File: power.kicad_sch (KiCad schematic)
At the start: 108 parts, among them U1 LT8350RV#PBF, U2 MP2386GG, U3 TPS65983BAZBHR

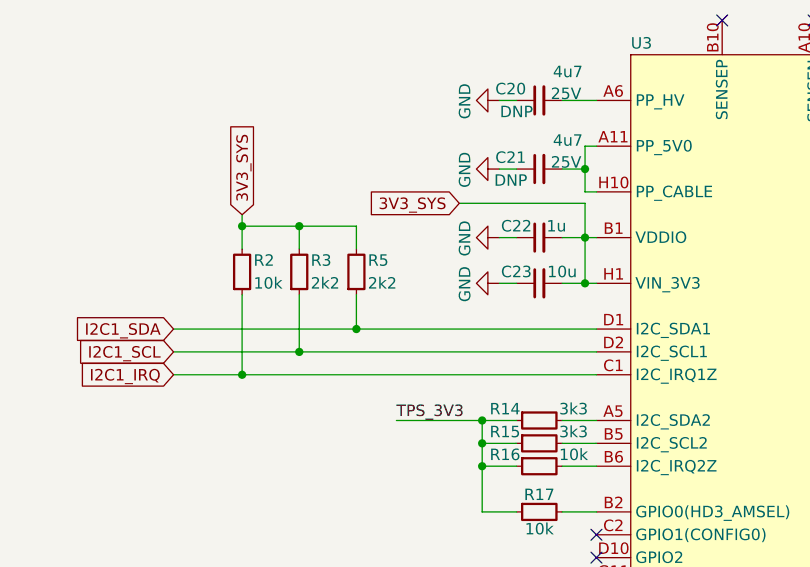
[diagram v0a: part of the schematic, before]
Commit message: Finished placement and routing of all TB controller related passives, finished routing of TB signals
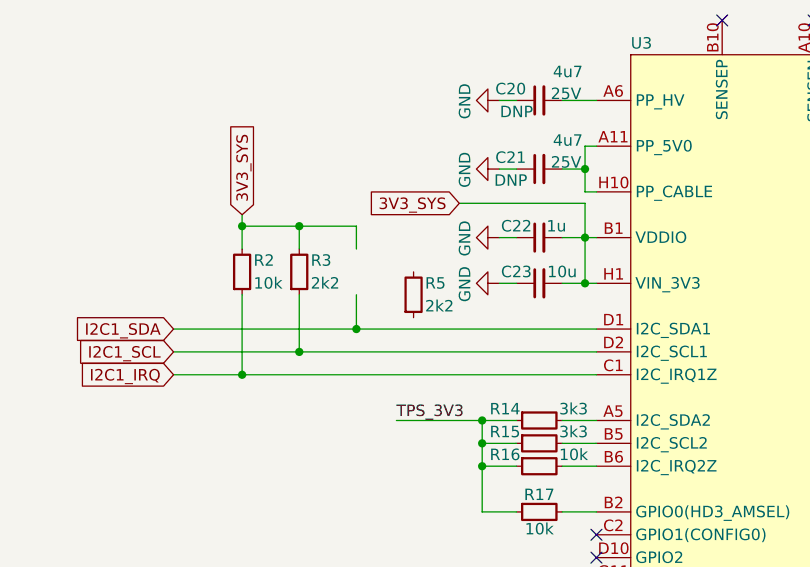
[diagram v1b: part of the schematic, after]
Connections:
- net 3V3_SYS: no longer R5.2
- net I2C1_SDA: no longer R5.1
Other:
- moved on the sheet: R5
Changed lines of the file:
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@@
     (pin "1")
   )
-  (symbol (lib_name "R_2k2_0402_1") (lib_id "antmicroResistors0402:R_2k2_0402") (at 95.25 68.58 90) (unit 1)
+  (symbol (lib_name "R_2k2_0402_1") (lib_id "antmicroResistors0402:R_2k2_0402") (at 101.6 71.12 90) (unit 1)
     (in_bom yes) (on_board yes)
-    (property "Reference" "R5" (id 0) (at 96.52 64.77 90)
+    (property "Reference" "R5" (id 0) (at 102.87 67.31 90)
       (effects (font (size 1.27 1.27) (thickness 0.15)) (justify right))
     )
-    (property "Value" "R_2k2_0402" (id 1) (at 107.95 48.26 0)
+    (property "Value" "R_2k2_0402" (id 1) (at 114.3 50.8 0)
       (effects (font (size 1.27 1.27) (thickness 0.15)) (justify left bottom) hide)
     )
-    (property "Footprint" "antmicro-footprints:R_0402_1005Metric" (id 2) (at 110.49 48.26 0)
+    (property "Footprint" "antmicro-footprints:R_0402_1005Metric" (id 2) (at 116.84 50.8 0)
       (effects (font (size 1.27 1.27) (thickness 0.15)) (justify left bottom) hide)
     )
-    (property "Datasheet" "https://www.bourns.com/docs/product-datasheets/cr.pdf" (id 3) (at 113.03 48.26 0)
+    (property "Datasheet" "https://www.bourns.com/docs/product-datasheets/cr.pdf" (id 3) (at 119.38 50.8 0)
       (effects (font (size 1.27 1.27) (thickness 0.15)) (justify left bottom) hide)
     )
-    (property "MPN" "CR0402-FX-2201GLF" (id 4) (at 115.57 48.26 0)
+    (property "MPN" "CR0402-FX-2201GLF" (id 4) (at 121.92 50.8 0)
       (effects (font (size 1.27 1.27) (thickness 0.15)) (justify left bottom) hide)
     )
-    (property "Manufacturer" "Bourns" (id 5) (at 118.11 48.26 0)
+    (property "Manufacturer" "Bourns" (id 5) (at 124.46 50.8 0)
       (effects (font (size 1.27 1.27) (thickness 0.15)) (justify left bottom) hide)
     )
-    (property "License" "Apache-2.0 License" (id 6) (at 120.65 48.26 0)
+    (property "License" "Apache-2.0 License" (id 6) (at 127 50.8 0)
       (effects (font (size 1.27 1.27) (thickness 0.15)) (justify left bottom) hide)
     )
-    (property "Copyright" "Copyright (c) 2023 Antmicro" (id 7) (at 123.19 48.26 0)
+    (property "Copyright" "Copyright (c) 2023 Antmicro" (id 7) (at 129.54 50.8 0)
       (effects (font (size 1.27 1.27) (thickness 0.15)) (justify left bottom) hide)
     )
-    (property "Val" "2k2" (id 8) (at 96.52 67.31 90)
+    (property "Val" "2k2" (id 8) (at 102.87 69.85 90)
       (effects (font (size 1.27 1.27) (thickness 0.15)) (justify right))
     )
-    (property "Tolerance" "1%" (id 9) (at 105.41 48.26 0)
+    (property "Tolerance" "1%" (id 9) (at 111.76 50.8 0)
       (effects (font (size 1.27 1.27)) (justify left bottom) hide)
     )

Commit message: Updated libraries, finished PCIe clock generator section
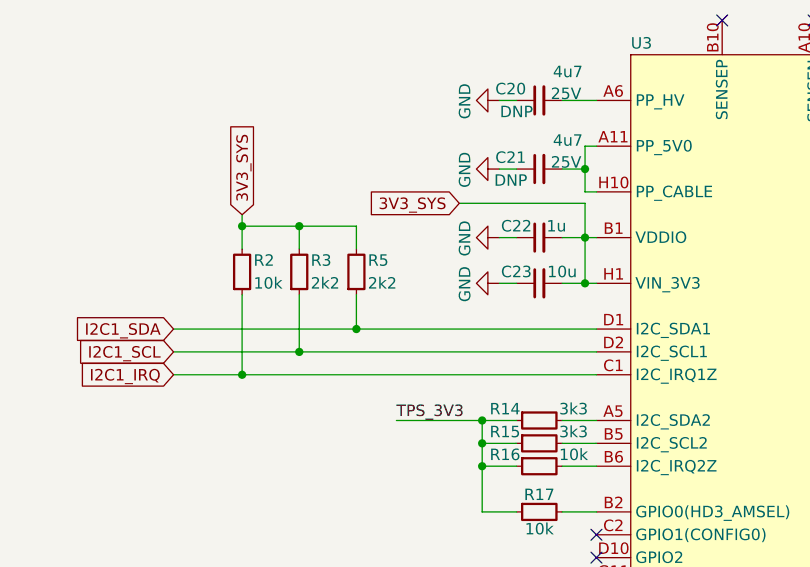
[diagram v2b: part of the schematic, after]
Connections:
- net 3V3_SYS: now also R5.2
- net I2C1_SDA: now also R5.1
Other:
- moved on the sheet: R5

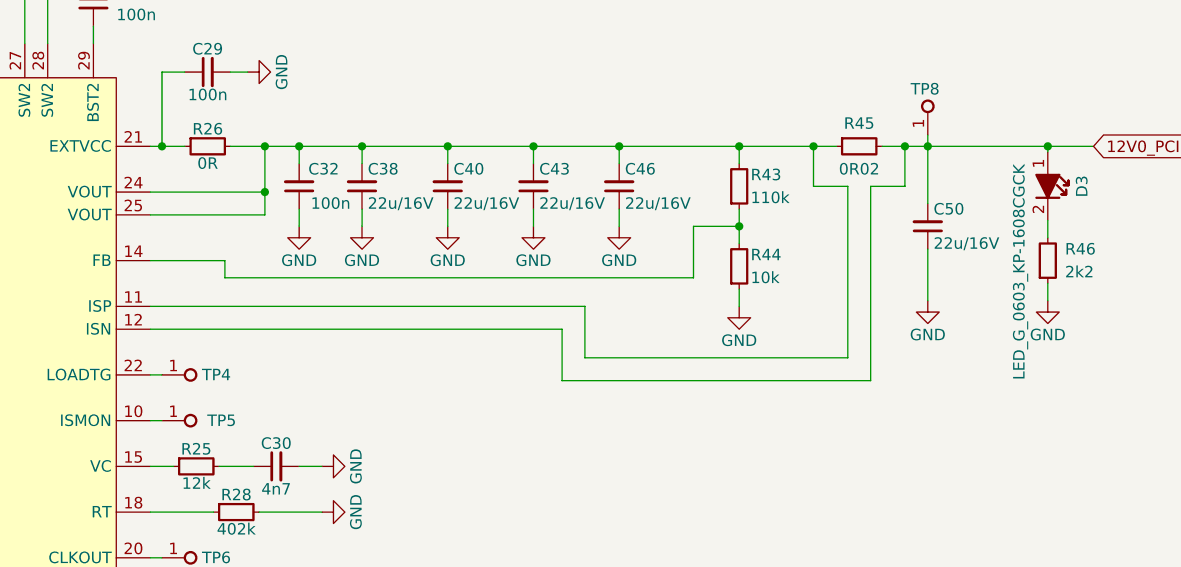
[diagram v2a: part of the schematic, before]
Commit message: Finished placing all DC-DC converters with all related components
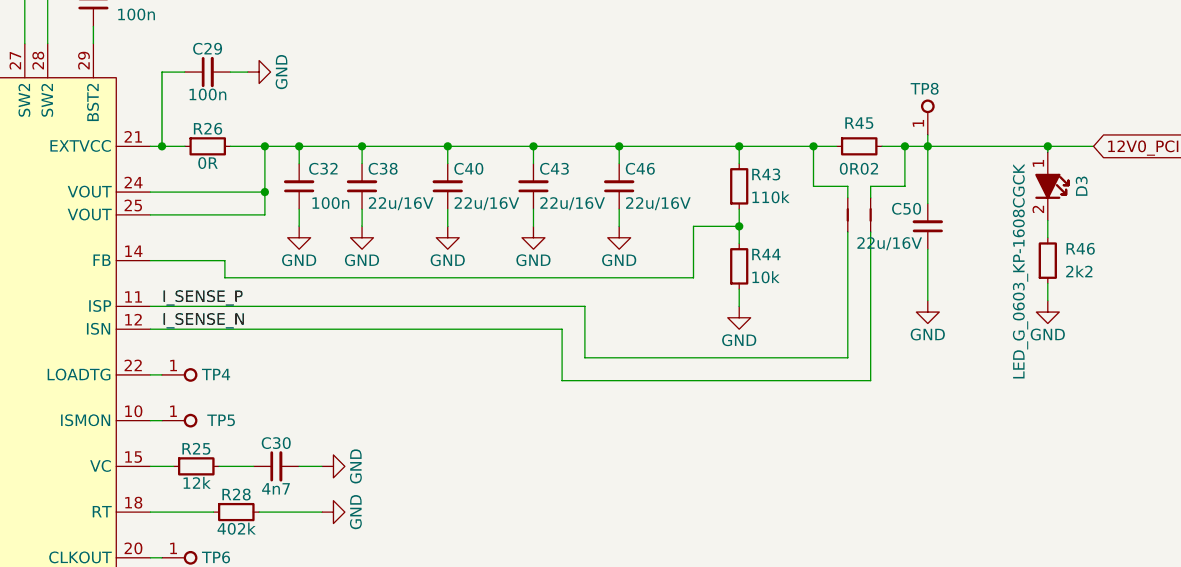
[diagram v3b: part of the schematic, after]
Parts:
- added TP10, TP11: Net-Tie_2, antmicro-footprints:NetTie-2_SMD_Pad0.127mm, symbol antmicroShuntsJumpers:Net-Tie_2
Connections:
- net 12V0_PCIE: now also TP11.2; no longer U1.12 (ISN)
- net at C32.2, C38.2, C40.2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: now also TP10.2; no longer U1.11 (ISP)
- new net I_SENSE_N: TP11.1, U1.12 (ISN)
- new net I_SENSE_P: TP10.1, U1.11 (ISP)
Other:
- moved on the sheet: C50
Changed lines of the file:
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@@
     (stroke (width 0) (type default) (color 0 0 0 0))
   )
+  (wire (pts (xy 242.57 240.03) (xy 242.57 241.3))
+    (stroke (width 0) (type default) (color 0 0 0 0))
+  )
   (wire (pts (xy 210.82 255.905) (xy 210.82 261.62))
     (stroke (width 0) (type default) (color 0 0 0 0))
@@
     (stroke (width 0) (type default) (color 0 0 0 0))
   )
+  (wire (pts (xy 245.11 245.11) (xy 245.11 261.62))
+    (stroke (width 0) (type default) (color 0 0 0 0))
+  )
   (wire (pts (xy 193.04 57.15) (xy 194.945 57.15))
     (stroke (width 0) (type default) (color 0 0 0 0))
   )
+  (wire (pts (xy 242.57 245.11) (xy 242.57 259.08))
+    (stroke (width 0) (type default) (color 0 0 0 0))
+  )
   (wire (pts (xy 120.015 148.59) (xy 121.92 148.59))
     (stroke (width 0) (type default) (color 0 0 0 0))
@@
     (stroke (width 0) (type default) (color 0 0 0 0))
   )
+  (wire (pts (xy 245.11 240.03) (xy 245.11 241.3))
+    (stroke (width 0) (type default) (color 0 0 0 0))
+  )
   (wire (pts (xy 88.9 60.96) (xy 88.9 63.5))
     (stroke (width 0) (type default) (color 0 0 0 0))
@@
     (stroke (width 0) (type default) (color 0 0 0 0))
   )
-  (wire (pts (xy 245.11 240.03) (xy 245.11 261.62))
-    (stroke (width 0) (type default) (color 0 0 0 0))
-  )
   (wire (pts (xy 149.86 344.17) (xy 152.4 344.17))
     (stroke (width 0) (type default) (color 0 0 0 0))
@@
     (stroke (width 0) (type default) (color 0 0 0 0))
   )
-  (wire (pts (xy 242.57 240.03) (xy 242.57 259.08))
-    (stroke (width 0) (type default) (color 0 0 0 0))
-  )
   (wire (pts (xy 33.655 229.87) (xy 40.005 229.87))
     (stroke (width 0) (type default) (color 0 0 0 0))
@@
     (effects (font (size 1.27 1.27)) (justify right bottom))
   )
+  (label "I_SENSE_P" (at 166.37 253.365 0)
+    (effects (font (size 1.27 1.27)) (justify left bottom))
+  )
   (label "TPS_3V3" (at 200.025 128.27 180)
     (effects (font (size 1.27 1.27)) (justify right bottom))
   )
+  (label "I_SENSE_N" (at 166.37 255.905 0)
+    (effects (font (size 1.27 1.27)) (justify left bottom))
+  )
   (label "SMPS_VREF" (at 185.42 286.385 180)
     (effects (font (size 1.27 1.27)) (justify right bottom))
@@
     (pin "2")
   )
+  (symbol (lib_id "antmicroShuntsJumpers:Net-Tie_2") (at 245.11 245.11 90) (unit 1)
+    (in_bom yes) (on_board yes) (fields_autoplaced)
+    (property "Reference" "TP11" (id 0) (at 246.38 241.9349 90)
+      (effects (font (size 1.27 1.27) (thickness 0.15)) (justify right) hide)
+    )
+    (property "Value" "Net-Tie_2" (id 1) (at 246.38 244.4749 90)
+      (effects (font (size 1.27 1.27) (thickness 0.15)) (justify right) hide)
+    )
+    (property "Footprint" "antmicro-footprints:NetTie-2_SMD_Pad0.127mm" (id 2) (at 250.19 223.52 0)
+      (effects (font (size 1.27 1.27) (thickness 0.15)) (justify left bottom) hide)
+    )
+    (property "Datasheet" "" (id 3) (at 252.73 223.52 0)
+      (effects (font (size 1.27 1.27) (thickness 0.15)) (justify left bottom) hide)
+    )
+    (property "Author" "Antmicro" (id 4) (at 260.35 223.52 0)
+      (effects (font (size 1.27 1.27) (thickness 0.15)) (justify left bottom) hide)
+    )
+    (property "License" "Apache-2.0" (id 5) (at 262.89 223.52 0)
+      (effects (font (size 1.27 1.27) (thickness 0.15)) (justify left bottom) hide)
+    )
+    (property "MPN" "" (id 6) (at 254 223.52 0)
+      (effects (font (size 1.27 1.27)) (justify left) hide)
+    )
+    (property "Manufacturer" "" (id 7) (at 256.54 223.52 0)
+      (effects (font (size 1.27 1.27)) (justify left) hide)
+    )
+    (pin "1")
+    (pin "2")
+  )
   (symbol (lib_id "power:GND") (at 124.46 363.22 0) (unit 1)
     (in_bom yes) (on_board yes)
@@
     (pin "2")
   )
-  (symbol (lib_id "antmicroCapacitors0603:C_22u_16V_0603") (at 251.46 247.015 90) (unit 1)
+  (symbol (lib_id "antmicroCapacitors0603:C_22u_16V_0603") (at 251.46 247.015 270) (mirror x) (unit 1)
     (in_bom yes) (on_board yes)
-    (property "Reference" "C50" (id 0) (at 252.095 242.57 90)
+    (property "Reference" "C50" (id 0) (at 250.825 242.57 90)
       (effects (font (size 1.27 1.27) (thickness 0.15)) (justify right))
     )
-    (property "Value" "C_22u_16V_0603" (id 1) (at 261.62 226.695 0)
+    (property "Value" "C_22u_16V_0603" (id 1) (at 241.3 226.695 0)
       (effects (font (size 1.27 1.27) (thickness 0.15)) (justify left bottom) hide)
     )
-    (property "Footprint" "antmicro-footprints:C_0603_1608Metric" (id 2) (at 264.16 226.695 0)
+    (property "Footprint" "antmicro-footprints:C_0603_1608Metric" (id 2) (at 238.76 226.695 0)
       (effects (font (size 1.27 1.27) (thickness 0.15)) (justify left bottom) hide)
     )
-    (property "Datasheet" "https://www.mouser.pl/datasheet/2/585/MLCC-1837944.pdf" (id 3) (at 266.7 226.695 0)
+    (property "Datasheet" "https://www.mouser.pl/datasheet/2/585/MLCC-1837944.pdf" (id 3) (at 236.22 226.695 0)
       (effects (font (size 1.27 1.27) (thickness 0.15)) (justify left bottom) hide)
     )
-    (property "MPN" "CL10A226MO7JZNC" (id 4) (at 269.24 226.695 0)
+    (property "MPN" "CL10A226MO7JZNC" (id 4) (at 233.68 226.695 0)
       (effects (font (size 1.27 1.27) (thickness 0.15)) (justify left bottom) hide)
     )
-    (property "Manufacturer" "Samsung" (id 5) (at 271.78 226.695 0)
+    (property "Manufacturer" "Samsung" (id 5) (at 231.14 226.695 0)
       (effects (font (size 1.27 1.27) (thickness 0.15)) (justify left bottom) hide)
     )
-    (property "License" "Apache-2.0 License" (id 6) (at 274.32 226.695 0)
+    (property "License" "Apache-2.0 License" (id 6) (at 228.6 226.695 0)
       (effects (font (size 1.27 1.27) (thickness 0.15)) (justify left bottom) hide)
     )
-    (property "Copyright" "Copyright (c) 2023 Antmicro" (id 7) (at 276.86 226.695 0)
+    (property "Copyright" "Copyright (c) 2023 Antmicro" (id 7) (at 226.06 226.695 0)
       (effects (font (size 1.27 1.27) (thickness 0.15)) (justify left bottom) hide)
     )
-    (property "Val" "22u/16V" (id 8) (at 252.095 246.38 90)
+    (property "Val" "22u/16V" (id 8) (at 250.825 246.38 90)
       (effects (font (size 1.27 1.27) (thickness 0.15)) (justify right))
     )
-    (property "Voltage" "" (id 9) (at 279.4 226.695 0)
+    (property "Voltage" "" (id 9) (at 223.52 226.695 0)
       (effects (font (size 1.27 1.27)) (justify left bottom) hide)
     )
-    (property "Dielectric" "" (id 10) (at 281.94 226.695 0)
+    (property "Dielectric" "" (id 10) (at 220.98 226.695 0)
       (effects (font (size 1.27 1.27)) (justify left bottom) hide)
     )
@@
     )
     (pin "1")
+    (pin "2")
+  )
+  (symbol (lib_id "antmicroShuntsJumpers:Net-Tie_2") (at 242.57 245.11 90) (unit 1)
+    (in_bom yes) (on_board yes) (fields_autoplaced)
+    (property "Reference" "TP10" (id 0) (at 243.84 241.9349 90)
+      (effects (font (size 1.27 1.27) (thickness 0.15)) (justify right) hide)
+    )
+    (property "Value" "Net-Tie_2" (id 1) (at 243.84 244.4749 90)
+      (effects (font (size 1.27 1.27) (thickness 0.15)) (justify right) hide)
+    )
+    (property "Footprint" "antmicro-footprints:NetTie-2_SMD_Pad0.127mm" (id 2) (at 247.65 223.52 0)
+      (effects (font (size 1.27 1.27) (thickness 0.15)) (justify left bottom) hide)
+    )
+    (property "Datasheet" "" (id 3) (at 250.19 223.52 0)
+      (effects (font (size 1.27 1.27) (thickness 0.15)) (justify left bottom) hide)
+    )
+    (property "Author" "Antmicro" (id 4) (at 257.81 223.52 0)
+      (effects (font (size 1.27 1.27) (thickness 0.15)) (justify left bottom) hide)
+    )
+    (property "License" "Apache-2.0" (id 5) (at 260.35 223.52 0)
+      (effects (font (size 1.27 1.27) (thickness 0.15)) (justify left bottom) hide)
+    )
+    (property "MPN" "" (id 6) (at 251.46 223.52 0)
+      (effects (font (size 1.27 1.27)) (justify left) hide)
+    )
+    (property "Manufacturer" "" (id 7) (at 254 223.52 0)
+      (effects (font (size 1.27 1.27)) (justify left) hide)
+    )
+    (pin "1")
